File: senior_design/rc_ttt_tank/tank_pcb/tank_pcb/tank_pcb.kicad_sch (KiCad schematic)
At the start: 40 parts, among them J1 TURRET, J2 FIRE, J3 DRIVING, J4 FW, J5 PWR, J6 PWR_TEST, Q1 NMOS, Q2 NMOS, U1 ESP32-DEVKIT-V1

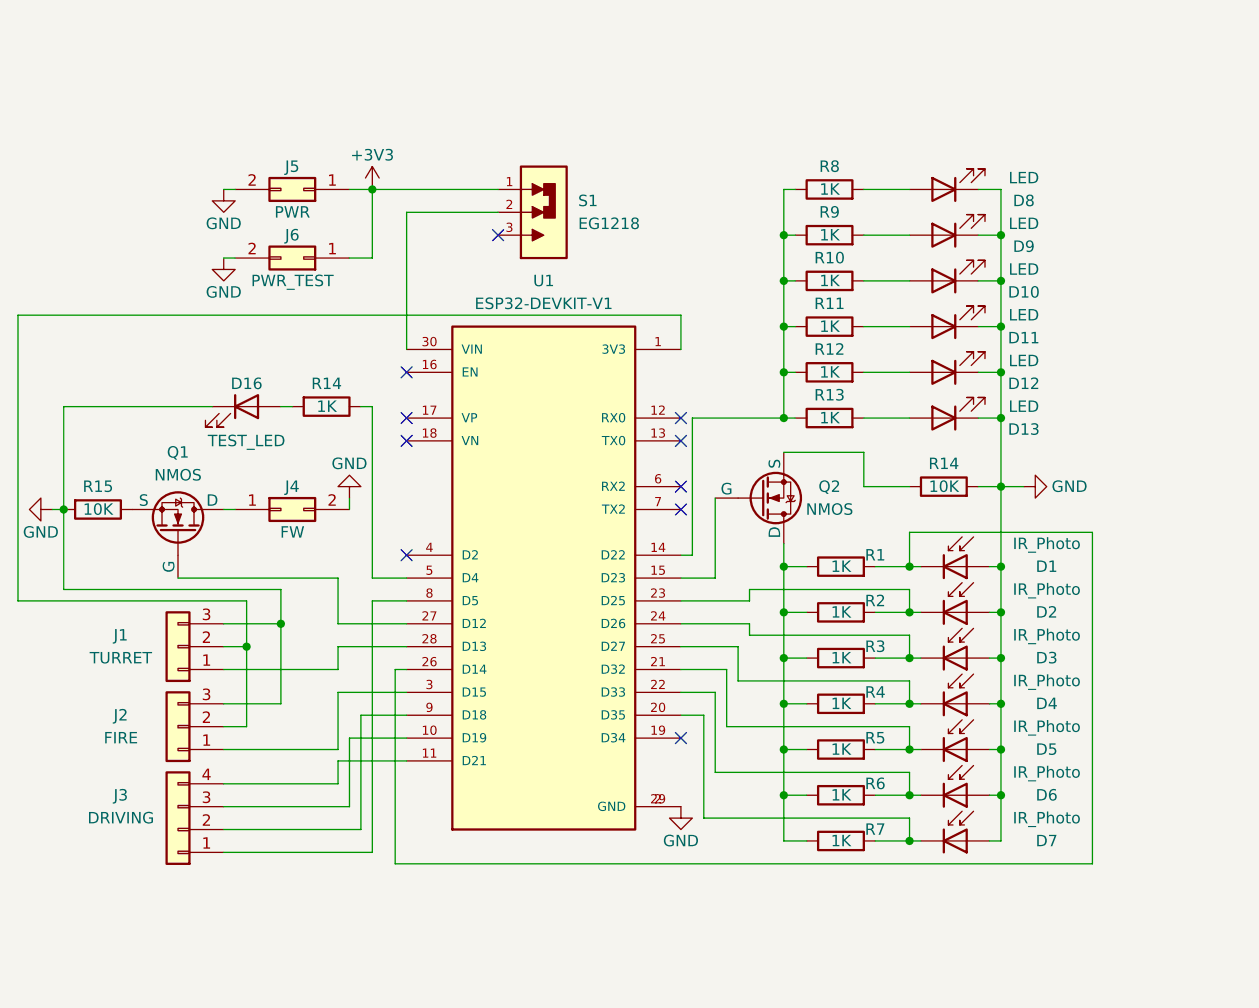
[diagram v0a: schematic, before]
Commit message: finished design the tank pcb
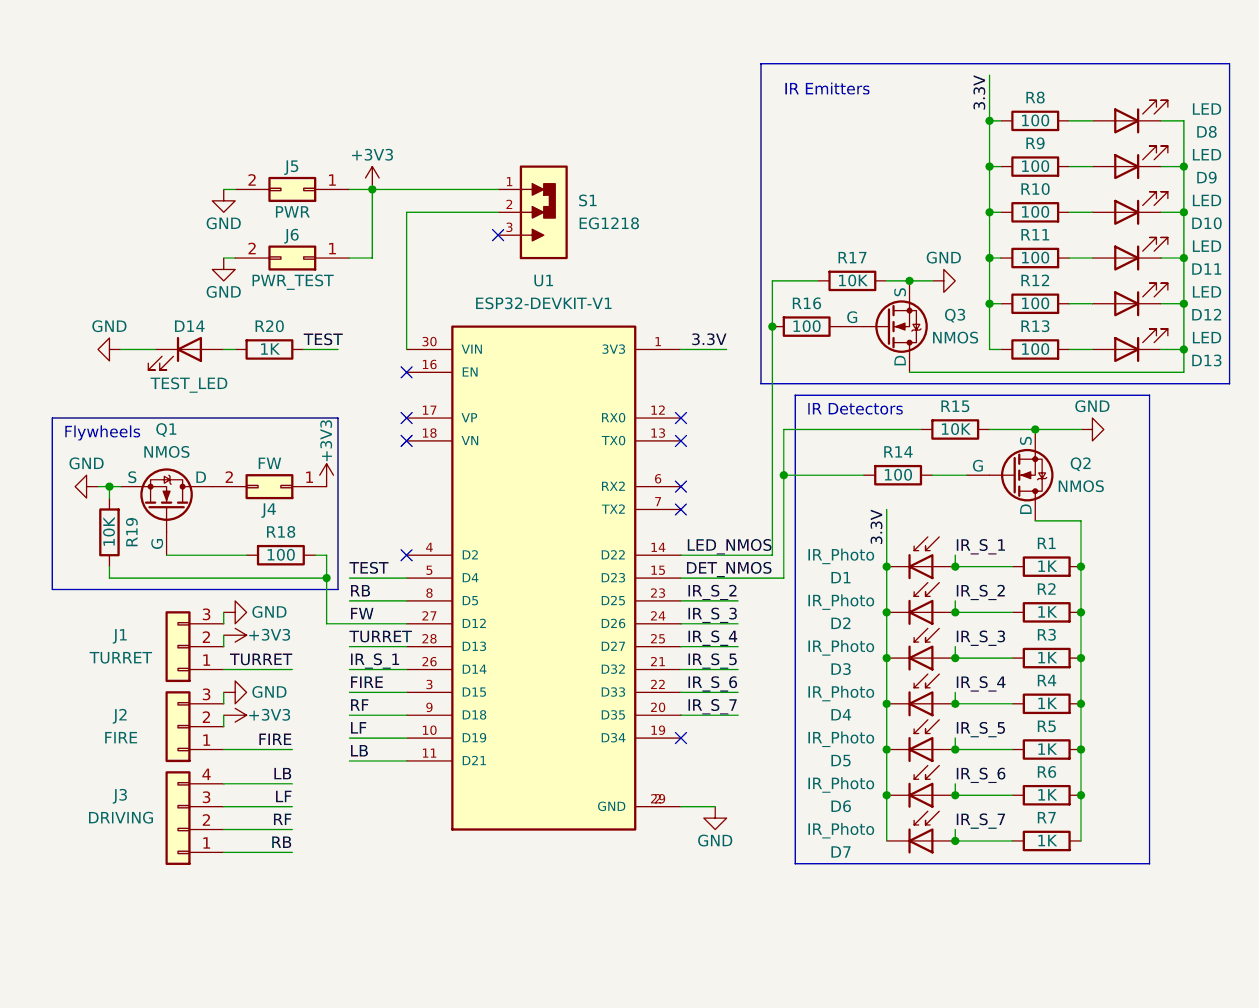
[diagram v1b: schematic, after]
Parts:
- added Q3: NMOS, 2N7002LT1G:SOT95P240X111-3N, symbol Simulation_SPICE:NMOS
- added R16, R18: 100, Resistor_THT:R_Axial_DIN0204_L3.6mm_D1.6mm_P7.62mm_Horizontal, symbol Device:R
- added R17, R19: 10K, Resistor_THT:R_Axial_DIN0204_L3.6mm_D1.6mm_P7.62mm_Horizontal, symbol Device:R
- D1, D10, D11, D12, D13, D2, D3, D4, D5, D6, D7, D8, D9: footprint (none) -> tank_pcb:LEDRD254W51D580H870
- D14: renamed from D16; footprint (none) -> LED_THT:LED_D3.0mm
- J1, J2: footprint (none) -> Connector_PinHeader_2.54mm:PinHeader_1x03_P2.54mm_Vertical
- J3: footprint (none) -> Connector_PinHeader_2.54mm:PinHeader_1x04_P2.54mm_Vertical
- Q1, Q2: footprint (none) -> 2N7002LT1G:SOT95P240X111-3N
- R1, R15, R2, R3, R4, R5, R6, R7: footprint (none) -> Resistor_THT:R_Axial_DIN0204_L3.6mm_D1.6mm_P7.62mm_Horizontal
- R10, R11, R12, R13, R8, R9: value 1K -> 100; footprint (none) -> Resistor_THT:R_Axial_DIN0204_L3.6mm_D1.6mm_P7.62mm_Horizontal
- R14: value 10K -> 100; footprint (none) -> Resistor_THT:R_Axial_DIN0204_L3.6mm_D1.6mm_P7.62mm_Horizontal
- R20: renamed from R14; footprint (none) -> Resistor_THT:R_Axial_DIN0204_L3.6mm_D1.6mm_P7.62mm_Horizontal
- S1: footprint EG1218:SW_EG1218 -> library_fp:SW_EG1218
- U1: footprint ESP32-DEVKIT-V1:MODULE_ESP32_DEVKIT_V1 -> library_fp:MODULE_ESP32_DEVKIT_V1
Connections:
- net +3V3: now also J1.2 (Pin_2), J2.2 (Pin_2), J4.1 (Pin_1)
- net GND: now also Q1.3 (S), Q2.3 (S), R15.1, Q3.3 (S), R17.1, R19.2; no longer D1.2 (A), D10.1 (K), D11.1 (K), D12.1 (K), D13.1 (K), D2.2 (A), D3.2 (A), D4.2 (A), D5.2 (A), D6.2 (A), D7.2 (A), D8.1 (K), D9.1 (K), J4.2 (Pin_2), R14.2, R15.2
- net at Q2.2 (G): now also R14.1; no longer U1.15 (D23)
- net 3.3V: now reaches R10.1, R11.1, R12.1, R13.1, R8.1, R9.1
- net 3.3V: now also D1.1 (K), D2.1 (K), D3.1 (K), D4.1 (K), D5.1 (K), D6.1 (K), D7.1 (K), U1.1 (3V3); no longer U1.14 (D22)
- net at Q1.1 (D): now also J4.2 (Pin_2); no longer J4.1 (Pin_1)
- net at Q1.2 (G): now also R18.2; no longer U1.27 (D12)
- net RB: now reaches J3.1 (Pin_1), U1.8 (D5)
- net RF: now reaches J3.2 (Pin_2), U1.9 (D18)
- net LF: now reaches J3.3 (Pin_3), U1.10 (D19)
- net LB: now reaches J3.4 (Pin_4), U1.11 (D21)
- net TEST: now reaches R20.1, U1.5 (D4)
- net FIRE: now reaches J2.1 (Pin_1), U1.3 (D15)
- net TURRET: now reaches J1.1 (Pin_1), U1.28 (D13)
- new net: D10.1 (K), D11.1 (K), D12.1 (K), D13.1 (K), D8.1 (K), D9.1 (K), Q3.1 (D)
- new net: Q2.1 (D), R1.2, R2.2, R3.2, R4.2, R5.2, R6.2, R7.2
- new net: Q3.2 (G), R16.1
- new net DET_NMOS: R14.2, R15.2, U1.15 (D23)
- new net FW: R18.1, R19.1, U1.27 (D12)
- new net IR_S_1: D1.2 (A), R1.1, U1.26 (D14)
- new net IR_S_2: D2.2 (A), R2.1, U1.23 (D25)
- new net IR_S_3: D3.2 (A), R3.1, U1.24 (D26)
- new net IR_S_4: D4.2 (A), R4.1, U1.25 (D27)
- new net IR_S_5: D5.2 (A), R5.1, U1.21 (D32)
- new net IR_S_6: D6.2 (A), R6.1, U1.22 (D33)
- new net IR_S_7: D7.2 (A), R7.1, U1.20 (D35)
- new net LED_NMOS: R16.2, R17.2, U1.14 (D22)
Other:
- note added: "Flywheels"
- note added: "IR Detectors"
- note added: "IR Emitters"
- moved on the sheet: D1, D10, D11, D12, D13, D14, D2, D3, D4, D5, D6, D7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

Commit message: Redesigned my tank pcb. Also got ADC output on sensor 1 and was able to detect IR light!
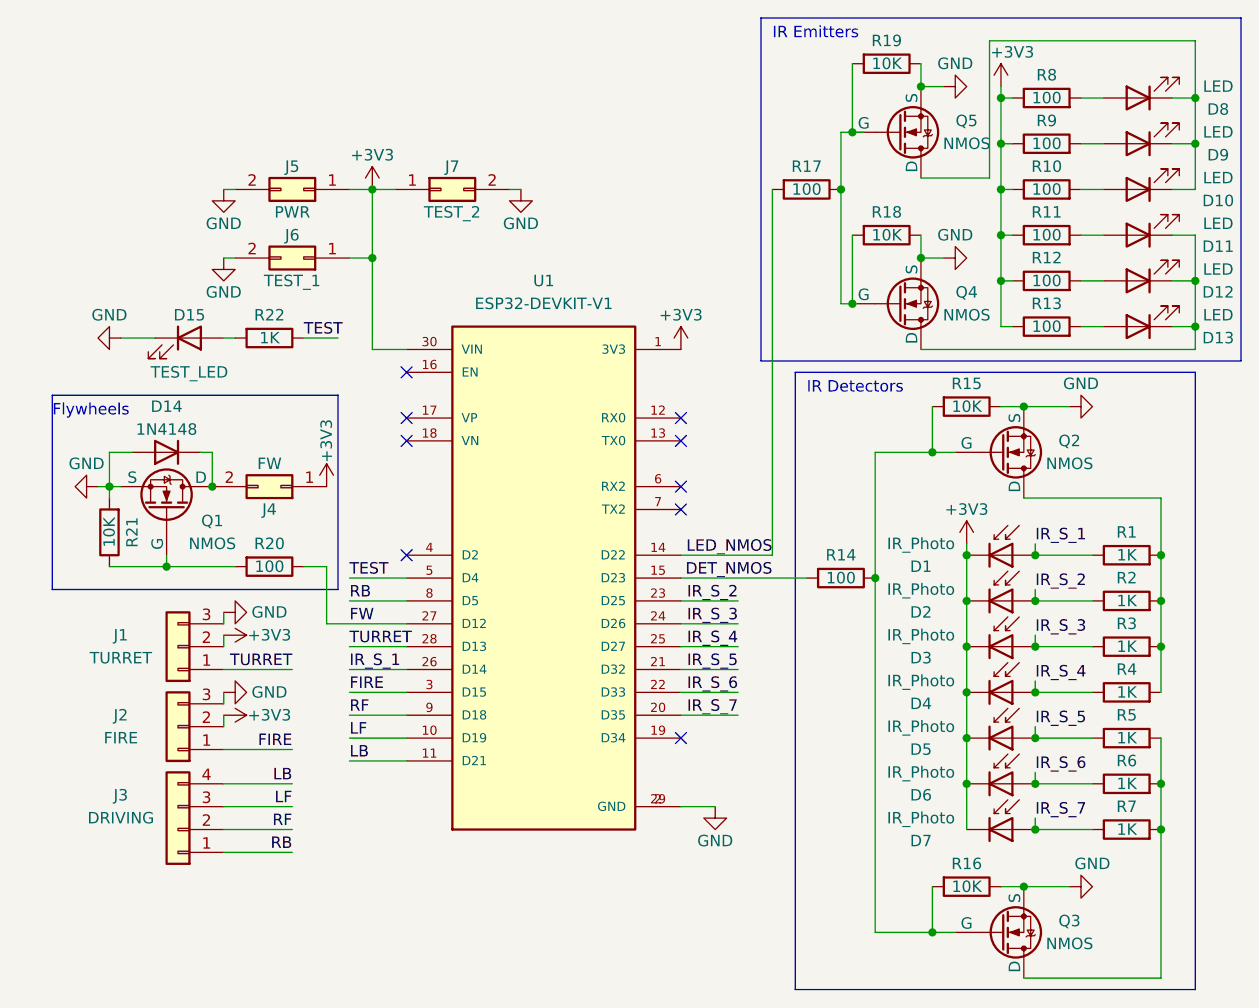
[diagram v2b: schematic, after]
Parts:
- removed S1: EG1218, library_fp:SW_EG1218, symbol EG1218:EG1218
- added D14: 1N4148, Diode_THT:D_DO-35_SOD27_P7.62mm_Horizontal, symbol Diode:1N4148
- added J7: TEST_2, Connector_PinHeader_2.54mm:PinHeader_1x02_P2.54mm_Vertical, symbol Connector_Generic:Conn_02x01
- added Q3, Q5: NMOS, 2N7002LT1G:SOT95P240X111-3N, symbol Simulation_SPICE:NMOS
- added R16, R19: 10K, Resistor_THT:R_Axial_DIN0204_L3.6mm_D1.6mm_P7.62mm_Horizontal, symbol Device:R
- J6: value PWR_TEST -> TEST_1
- renumbered D14 to D15, Q3 to Q4, R16 to R17, R17 to R18, R18 to R20, R19 to R21, R20 to R22
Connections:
- net 3.3V is gone; now on net +3V3: D1.1 (K), D2.1 (K), D3.1 (K), D4.1 (K), D5.1 (K), D6.1 (K), D7.1 (K), R10.1, R11.1, R12.1, R13.1, R8.1, R9.1, U1.1 (3V3)
- net +3V3: now also U1.30 (VIN), J7.1 (Pin_1)
- net DET_NMOS: no longer R15.2
- net FW: no longer R21.1
- net GND: now also D14.2 (A), J7.2 (Pin_2), Q3.3 (S), Q5.3 (S), R16.1, R19.1
- net LED_NMOS: no longer R18.2
- net at D11.1 (K), D12.1 (K), D13.1 (K)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: no longer D10.1 (K), D8.1 (K), D9.1 (K)
- net at Q2.1 (D), R1.2, R2.2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: no longer R5.2, R6.2, R7.2
- net at Q2.2 (G), R14.1: now also R15.2, Q3.2 (G), R16.2
- net at J4.2 (Pin_2), Q1.1 (D): now also D14.1 (K)
- net at Q1.2 (G), R20.2: now also R21.1
- net at Q4.2 (G), R17.1: now also R18.2, Q5.2 (G), R19.2
- new net: D10.1 (K), D8.1 (K), D9.1 (K), Q5.1 (D)
- new net: Q3.1 (D), R5.2, R6.2, R7.2
- no-connect marks 10 -> 9
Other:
- moved on the sheet: D1, D10, D11, D12, D13, D15, D2, D3, D4, D5, D6, D7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

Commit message: driving and firing works. algorithm is still too long needs to be broken up. Transistors don't work still
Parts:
- R1, R2, R3, R4, R5, R6, R7: value 1K -> 10K
- R10, R11, R12, R13, R8, R9: value 100 -> 47
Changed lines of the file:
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@@
       (effects (font (size 1.27 1.27)))
     )
-    (property "Value" "1K" (at 213.36 104.14 90)
+    (property "Value" "10K" (at 213.36 104.14 90)
       (effects (font (size 1.27 1.27)))
     )
@@
       (effects (font (size 1.27 1.27)))
     )
-    (property "Value" "100" (at 204.47 43.18 90)
+    (property "Value" "47" (at 204.47 43.18 90)
       (effects (font (size 1.27 1.27)))
     )
@@
       (effects (font (size 1.27 1.27)))
     )
-    (property "Value" "1K" (at 213.36 109.22 90)
+    (property "Value" "10K" (at 213.36 109.22 90)
       (effects (font (size 1.27 1.27)))
     )
@@
       (effects (font (size 1.27 1.27)))
     )
-    (property "Value" "1K" (at 213.36 99.06 90)
+    (property "Value" "10K" (at 213.36 99.06 90)
       (effects (font (size 1.27 1.27)))
     )
@@
   )
   (symbol (lib_id "Device:R") (at 213.36 124.46 90) (unit 1)
-    (in_bom yes) (on_board yes) (dnp no)
+    (in_bom yes) (on_board yes) (dnp no) (fields_autoplaced)
     (property "Reference" "R7" (at 213.36 121.92 90)
       (effects (font (size 1.27 1.27)))
     )
-    (property "Value" "1K" (at 213.36 124.46 90)
+    (property "Value" "10K" (at 213.36 124.46 90)
       (effects (font (size 1.27 1.27)))
     )
@@
       (effects (font (size 1.27 1.27)))
     )
-    (property "Value" "100" (at 204.47 48.26 90)
+    (property "Value" "47" (at 204.47 48.26 90)
       (effects (font (size 1.27 1.27)))
     )
@@
       (effects (font (size 1.27 1.27)))
     )
-    (property "Value" "100" (at 204.47 58.42 90)
+    (property "Value" "47" (at 204.47 58.42 90)
       (effects (font (size 1.27 1.27)))
     )
@@
       (effects (font (size 1.27 1.27)))
     )
-    (property "Value" "100" (at 204.47 63.5 90)
+    (property "Value" "47" (at 204.47 63.5 90)
       (effects (font (size 1.27 1.27)))
     )
@@
       (effects (font (size 1.27 1.27)))
     )
-    (property "Value" "1K" (at 213.36 93.98 90)
+    (property "Value" "10K" (at 213.36 93.98 90)
       (effects (font (size 1.27 1.27)))
     )
@@
       (effects (font (size 1.27 1.27)))
     )
-    (property "Value" "100" (at 204.47 53.34 90)
+    (property "Value" "47" (at 204.47 53.34 90)
       (effects (font (size 1.27 1.27)))
     )
@@
       (effects (font (size 1.27 1.27)))
     )
-    (property "Value" "1K" (at 213.36 114.3 90)
+    (property "Value" "10K" (at 213.36 114.3 90)
       (effects (font (size 1.27 1.27)))
     )
@@
       (effects (font (size 1.27 1.27)))
     )
-    (property "Value" "100" (at 204.47 68.58 90)
+    (property "Value" "47" (at 204.47 68.58 90)
       (effects (font (size 1.27 1.27)))
     )
@@
       (effects (font (size 1.27 1.27)))
     )
-    (property "Value" "1K" (at 213.36 119.38 90)
-      (effects (font (size 1.27 1.27)))
-    )
+    (property "Value" "10K" (at 213.36 119.38 90)
+      (effects (font (size 1.27 1.27)))
+    )
